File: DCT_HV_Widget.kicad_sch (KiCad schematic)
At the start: 23 parts, among them J1 Control Voltage, J2 Bench Power Supply, J3 High Voltage, Q1 ZXTN10150D, U1 LT1468CS8-PBF, U2 OC150G

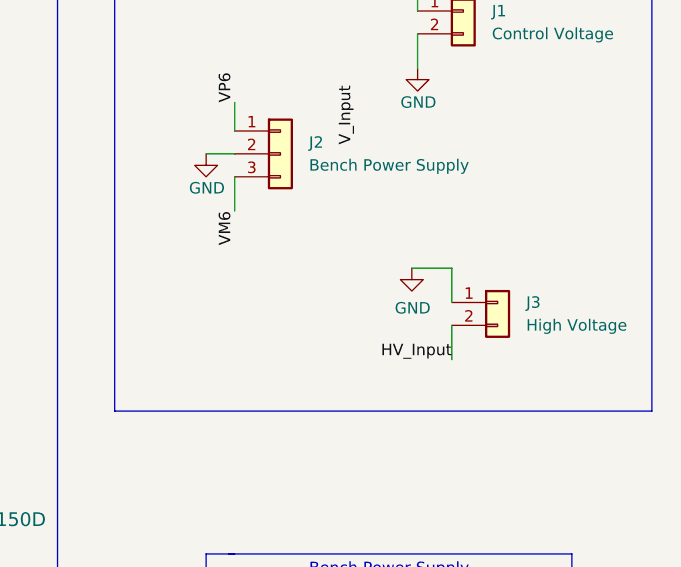
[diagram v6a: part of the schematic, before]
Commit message: Updated PCB with Gerard feedback
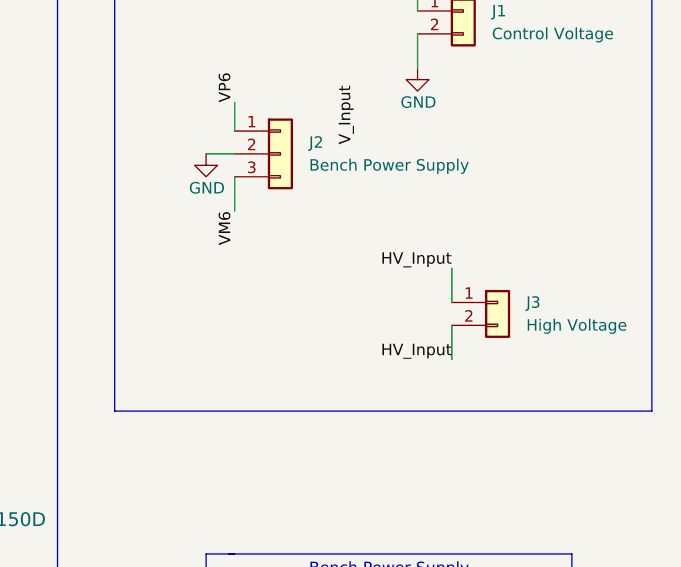
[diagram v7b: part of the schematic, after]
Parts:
- R5: footprint Resistor_SMD:R_0603_1608Metric -> Resistor_THT:R_Axial_DIN0207_L6.3mm_D2.5mm_P10.16mm_Horizontal
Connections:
- net GND: no longer J3.1 (Pin_1)
- net HV_Input: now also J3.1 (Pin_1)
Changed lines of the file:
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@@
-    (stroke (width 0) (type default) (color 0 0 0 0))
-  )
-  (wire (pts (xy 234.95 60.325) (xy 239.395 60.325))
     (stroke (width 0) (type default) (color 0 0 0 0))
   )
@@
   (label "HV_Input" (at 125.095 137.795 0)
     (effects (font (size 1.27 1.27)) (justify left bottom))
+  )
+  (label "HV_Input" (at 239.395 60.325 180)
+    (effects (font (size 1.27 1.27)) (justify right bottom))
   )
   (label "V_Input" (at 228.6 40.005 270)
@@
     (pin "2")
   )
-  (symbol (lib_id "power:GND") (at 234.95 60.325 0) (unit 1)
-    (in_bom yes) (on_board yes)
-    (property "Reference" "#PWR0106" (id 0) (at 234.95 66.675 0)
-      (effects (font (size 1.27 1.27)) hide)
-    )
-    (property "Value" "GND" (id 1) (at 233.045 64.77 0)
-      (effects (font (size 1.27 1.27)) (justify left))
-    )
-    (property "Footprint" "" (id 2) (at 234.95 60.325 0)
-      (effects (font (size 1.27 1.27)) hide)
-    )
-    (property "Datasheet" "" (id 3) (at 234.95 60.325 0)
-      (effects (font (size 1.27 1.27)) hide)
-    )
-    (pin "1")
-  )
   (symbol (lib_id "Device:R_Small_US") (at 178.435 105.41 0) (unit 1)
     (in_bom yes) (on_board yes) (fields_autoplaced)
@@
       (effects (font (size 1.27 1.27)) (justify left))
     )
-    (property "Footprint" "Resistor_SMD:R_0603_1608Metric" (id 2) (at 178.435 105.41 0)
+    (property "Footprint" "Resistor_THT:R_Axial_DIN0207_L6.3mm_D2.5mm_P10.16mm_Horizontal" (id 2) (at 178.435 105.41 0)
       (effects (font (size 1.27 1.27)) hide)
     )
@@
       (reference "#PWR0105") (unit 1) (value "GND") (footprint "")
     )
-    (path "/595337c3-7abb-4c23-a055-91bf831bbb77"
-      (reference "#PWR0106") (unit 1) (value "GND") (footprint "")
-    )
     (path "/d7412664-fb55-4327-9567-f6e1a4f37fe6"
       (reference "#PWR0108") (unit 1) (value "GND") (footprint "")
@@
     )
     (path "/5c3a777b-7dd9-4654-b56a-cdd0b8dc91a4"
-      (reference "R5") (unit 1) (value "90.9") (footprint "Resistor_SMD:R_0603_1608Metric")
+      (reference "R5") (unit 1) (value "90.9") (footprint "Resistor_THT:R_Axial_DIN0207_L6.3mm_D2.5mm_P10.16mm_Horizontal")
     )
     (path "/829701ec-08f3-4bc3-ab1b-2b279ba51178"
